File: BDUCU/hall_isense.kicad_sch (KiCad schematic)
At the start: 1 part, among them U6 LM358

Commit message: BDUCU did stuffs
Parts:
- added C15: 0.1uF, RMC_Capacitor:C_0805_2012Metric_Pad1.18x1.45mm_HandSolder_L, symbol Device:C
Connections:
- net HALL_HI_input: now reaches U6.5 (+)
- net HALL_HI: now reaches U6.6 (-)
- net HALL_HI: now also U6.7
- net GND: now reaches U6.4 (V-)
- net GND: now also C15.2
- net +5V: now reaches U6.8 (V+)
- net +5V: now also C15.1
- net HALL_LO: now reaches U6.1
- net HALL_LO: now also U6.2 (-)
- net HALL_LO_input: now reaches U6.3 (+)
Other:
- moved on the sheet: U6C
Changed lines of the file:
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@@
 (kicad_sch (version 20230121) (generator eeschema)
   (paper "A4")
-  (symbol (lib_id "Amplifier_Operational:LM358") (at 116.078 89.916 0) (unit 2)
-    (in_bom yes) (on_board yes) (dnp no) (fields_autoplaced)
-    (property "Reference" "U6" (at 116.078 80.01 0)
-      (effects (font (size 1.27 1.27)))
-    )
-    (property "Value" "LM358" (at 116.078 82.55 0)
-      (effects (font (size 1.27 1.27)))
-    )
-    (property "Footprint" "Package_SO:SOIC-8_3.9x4.9mm_P1.27mm" (at 116.078 89.916 0)
-      (effects (font (size 1.27 1.27)) hide)
-    )
-    (property "Datasheet" "http://www.ti.com/lit/ds/symlink/lm2904-n.pdf" (at 116.078 89.916 0)
+  (junction (at 149.86 38.1) (diameter 0) (color 0 0 0 0)
+  )
+  (junction (at 149.86 53.34) (diameter 0) (color 0 0 0 0)
+  )
+  (wire (pts (xy 144.145 53.34) (xy 149.86 53.34))
+    (stroke (width 0) (type default))
+  )
+  (wire (pts (xy 108.585 72.39) (xy 108.585 76.2))
+    (stroke (width 0) (type default))
+  )
+  (wire (pts (xy 144.145 42.545) (xy 144.145 38.1))
+    (stroke (width 0) (type default))
+  )
+  (wire (pts (xy 123.825 76.2) (xy 123.825 69.85))
+    (stroke (width 0) (type default))
+  )
+  (wire (pts (xy 108.585 76.2) (xy 123.825 76.2))
+    (stroke (width 0) (type default))
+  )
+  (wire (pts (xy 144.145 38.1) (xy 149.86 38.1))
+    (stroke (width 0) (type default))
+  )
+  (wire (pts (xy 108.585 97.79) (xy 123.825 97.79))
+    (stroke (width 0) (type default))
+  )
+  (wire (pts (xy 108.585 92.71) (xy 108.585 97.79))
+    (stroke (width 0) (type default))
+  )
+  (wire (pts (xy 123.825 97.79) (xy 123.825 90.17))
+    (stroke (width 0) (type default))
+  )
+  (wire (pts (xy 144.145 50.165) (xy 144.145 53.34))
+    (stroke (width 0) (type default))
+  )
+  (global_label "HALL_HI" (shape input) (at 123.825 90.17 0) (fields_autoplaced)
+    (effects (font (size 1.27 1.27)) (justify left))
+    (property "Intersheetrefs" "${INTERSHEET_REFS}" (at 134.1884 90.17 0)
+      (effects (font (size 1.27 1.27)) (justify left) hide)
+    )
+  )
+  (global_label "HALL_HI_input" (shape input) (at 108.585 87.63 180) (fields_autoplaced)
+    (effects (font (size 1.27 1.27)) (justify right))
+    (property "Intersheetrefs" "${INTERSHEET_REFS}" (at 92.4765 87.63 0)
+      (effects (font (size 1.27 1.27)) (justify right) hide)
+    )
+  )
+  (global_label "HALL_LO" (shape input) (at 123.825 69.85 0) (fields_autoplaced)
+    (effects (font (size 1.27 1.27)) (justify left))
+    (property "Intersheetrefs" "${INTERSHEET_REFS}" (at 134.6117 69.85 0)
+      (effects (font (size 1.27 1.27)) (justify left) hide)
+    )
+  )
+  (global_label "HALL_LO_input" (shape input) (at 108.585 67.31 180) (fields_autoplaced)
+    (effects (font (size 1.27 1.27)) (justify right))
+    (property "Intersheetrefs" "${INTERSHEET_REFS}" (at 92.0532 67.31 0)
+      (effects (font (size 1.27 1.27)) (justify right) hide)
+    )
+  )
+  (symbol (lib_id "power:GND") (at 149.86 53.34 0) (unit 1)
+    (in_bom yes) (on_board yes) (dnp no) (fields_autoplaced)
+    (property "Reference" "#PWR055" (at 149.86 59.69 0)
+      (effects (font (size 1.27 1.27)) hide)
+    )
+    (property "Value" "GND" (at 149.86 58.42 0)
+      (effects (font (size 1.27 1.27)))
+    )
+    (property "Footprint" "" (at 149.86 53.34 0)
+      (effects (font (size 1.27 1.27)) hide)
+    )
+    (property "Datasheet" "" (at 149.86 53.34 0)
+      (effects (font (size 1.27 1.27)) hide)
+    )
+    (pin "1")
+    (instances
+      (project "BDUCU"
+        (path "/9942a424-e19d-4ffb-8473-f960b5c811cf/8fc427df-2d97-44b9-b479-5014f2f05880/146987db-cc4e-40c2-bab5-0abba2715ce3"
+          (reference "#PWR055") (unit 1)
+        )
+        (path "/9942a424-e19d-4ffb-8473-f960b5c811cf/8fc427df-2d97-44b9-b479-5014f2f05880/e4047b2f-bef8-49d9-83e0-04d733111886"
+          (reference "#PWR058") (unit 1)
+        )
+        (path "/9942a424-e19d-4ffb-8473-f960b5c811cf/6945656a-1a27-4b96-8a88-6a11e7484dc7"
+          (reference "#PWR066") (unit 1)
+        )
+      )
+    )
+  )
+  (symbol (lib_id "Amplifier_Operational:LM358") (at 116.205 90.17 0) (unit 2)
+    (in_bom yes) (on_board yes) (dnp no) (fields_autoplaced)
+    (property "Reference" "U6" (at 116.205 80.264 0)
+      (effects (font (size 1.27 1.27)))
+    )
+    (property "Value" "LM358" (at 116.205 82.804 0)
+      (effects (font (size 1.27 1.27)))
+    )
+    (property "Footprint" "Package_SO:SOIC-8_3.9x4.9mm_P1.27mm" (at 116.205 90.17 0)
+      (effects (font (size 1.27 1.27)) hide)
+    )
+    (property "Datasheet" "http://www.ti.com/lit/ds/symlink/lm2904-n.pdf" (at 116.205 90.17 0)
       (effects (font (size 1.27 1.27)) hide)
     )
@@
     )
   )
-  (symbol (lib_id "Amplifier_Operational:LM358") (at 207.772 136.652 0) (unit 3)
-    (in_bom yes) (on_board yes) (dnp no) (fields_autoplaced)
-    (property "Reference" "U6" (at 207.01 135.382 0)
+  (symbol (lib_id "Device:C") (at 144.145 46.355 0) (unit 1)
+    (in_bom yes) (on_board yes) (dnp no)
+    (property "Reference" "C15" (at 140.081 45.085 0)
+      (effects (font (size 1.27 1.27)) (justify right))
+    )
+    (property "Value" "0.1uF" (at 140.081 47.625 0)
+      (effects (font (size 1.27 1.27)) (justify right))
+    )
+    (property "Footprint" "RMC_Capacitor:C_0805_2012Metric_Pad1.18x1.45mm_HandSolder_L" (at 145.1102 50.165 0)
+      (effects (font (size 1.27 1.27)) hide)
+    )
+    (property "Datasheet" "~" (at 144.145 46.355 0)
+      (effects (font (size 1.27 1.27)) hide)
+    )
+    (pin "1")
+    (pin "2")
+    (instances
+      (project "BDUCU"
+        (path "/9942a424-e19d-4ffb-8473-f960b5c811cf/d0210ccf-eb84-46ca-8cbf-aeaae330deeb"
+          (reference "C15") (unit 1)
+        )
+        (path "/9942a424-e19d-4ffb-8473-f960b5c811cf/6945656a-1a27-4b96-8a88-6a11e7484dc7"
+          (reference "C31") (unit 1)
+        )
+      )
+    )
+  )
+  (symbol (lib_id "power:+5V") (at 149.86 38.1 0) (unit 1)
+    (in_bom yes) (on_board yes) (dnp no) (fields_autoplaced)
+    (property "Reference" "#PWR014" (at 149.86 41.91 0)
+      (effects (font (size 1.27 1.27)) hide)
+    )
+    (property "Value" "+5V" (at 149.86 33.782 0)
+      (effects (font (size 1.27 1.27)))
+    )
+    (property "Footprint" "" (at 149.86 38.1 0)
+      (effects (font (size 1.27 1.27)) hide)
+    )
+    (property "Datasheet" "" (at 149.86 38.1 0)
+      (effects (font (size 1.27 1.27)) hide)
+    )
+    (pin "1")
+    (instances
+      (project "BDUCU"
+        (path "/9942a424-e19d-4ffb-8473-f960b5c811cf/d0210ccf-eb84-46ca-8cbf-aeaae330deeb"
+          (reference "#PWR014") (unit 1)
+        )
+        (path "/9942a424-e19d-4ffb-8473-f960b5c811cf/6945656a-1a27-4b96-8a88-6a11e7484dc7"
+          (reference "#PWR065") (unit 1)
+        )
+      )
+    )
+  )
+  (symbol (lib_id "Amplifier_Operational:LM358") (at 152.4 45.72 0) (unit 3)
+    (in_bom yes) (on_board yes) (dnp no) (fields_autoplaced)
+    (property "Reference" "U6" (at 151.638 44.45 0)
       (effects (font (size 1.27 1.27)) (justify left))
     )
-    (property "Value" "LM358" (at 207.01 137.922 0)
+    (property "Value" "LM358" (at 151.638 46.99 0)
       (effects (font (size 1.27 1.27)) (justify left))
     )
-    (property "Footprint" "Package_SO:SOIC-8_3.9x4.9mm_P1.27mm" (at 207.772 136.652 0)
-      (effects (font (size 1.27 1.27)) hide)
-    )
-    (property "Datasheet" "http://www.ti.com/lit/ds/symlink/lm2904-n.pdf" (at 207.772 136.652 0)
+    (property "Footprint" "Package_SO:SOIC-8_3.9x4.9mm_P1.27mm" (at 152.4 45.72 0)
+      (effects (font (size 1.27 1.27)) hide)
+    )
+    (property "Datasheet" "http://www.ti.com/lit/ds/symlink/lm2904-n.pdf" (at 152.4 45.72 0)
       (effects (font (size 1.27 1.27)) hide)
     )
@@
     )
   )
-  (symbol (lib_id "Amplifier_Operational:LM358") (at 116.332 69.85 0) (unit 1)
-    (in_bom yes) (on_board yes) (dnp no) (fields_autoplaced)
-    (property "Reference" "U6" (at 116.332 60.198 0)
-      (effects (font (size 1.27 1.27)))
-    )
-    (property "Value" "LM358" (at 116.332 62.738 0)
-      (effects (font (size 1.27 1.27)))
-    )
-    (property "Footprint" "Package_SO:SOIC-8_3.9x4.9mm_P1.27mm" (at 116.332 69.85 0)
-      (effects (font (size 1.27 1.27)) hide)
-    )
-    (property "Datasheet" "http://www.ti.com/lit/ds/symlink/lm2904-n.pdf" (at 116.332 69.85 0)
-      (effects (font (size 1.27 1.27)) hide)
-    )
+  (symbol (lib_id "Amplifier_Operational:LM358") (at 116.205 69.85 0) (unit 1)
+    (in_bom yes) (on_board yes) (dnp no) (fields_autoplaced)
+    (property "Reference" "U6" (at 116.205 60.198 0)
+      (effects (font (size 1.27 1.27)))
+    )
+    (property "Value" "LM358" (at 116.205 62.738 0)
+      (effects (font (size 1.27 1.27)))
+    )
+    (property "Footprint" "Package_SO:SOIC-8_3.9x4.9mm_P1.27mm" (at 116.205 69.85 0)
+      (effects (font (size 1.27 1.27)) hide)
+    )
+    (property "Datasheet" "http://www.ti.com/lit/ds/symlink/lm2904-n.pdf" (at 116.205 69.85 0)
+      (effects (font (size 1.27 1.27)) hide)
+    )

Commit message: weeeeeeee
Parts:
- renumbered C15 to C31

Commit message: bducu scheme done, waiting for check
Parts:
- C31: value 0.1uF -> 100nF
- U6: footprint Package_SO:SOIC-8_3.9x4.9mm_P1.27mm -> RMC_SO:SOIC-8_3.9x4.9mm_P1.27mm_RMC_Handsolder
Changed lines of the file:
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@@
 			)
 		)
-		(property "Footprint" "Package_SO:SOIC-8_3.9x4.9mm_P1.27mm"
+		(property "Footprint" "RMC_SO:SOIC-8_3.9x4.9mm_P1.27mm_RMC_Handsolder"
 			(at 116.205 90.17 0)
 			(effects
@@
 			)
 		)
-		(property "Value" "0.1uF"
+		(property "Value" "100nF"
 			(at 140.081 47.625 0)
 			(effects
@@
 			)
 		)
-		(property "Footprint" "Package_SO:SOIC-8_3.9x4.9mm_P1.27mm"
+		(property "Footprint" "RMC_SO:SOIC-8_3.9x4.9mm_P1.27mm_RMC_Handsolder"
 			(at 152.4 45.72 0)
 			(effects
@@
 			)
 		)
-		(property "Footprint" "Package_SO:SOIC-8_3.9x4.9mm_P1.27mm"
+		(property "Footprint" "RMC_SO:SOIC-8_3.9x4.9mm_P1.27mm_RMC_Handsolder"
 			(at 116.205 69.85 0)
 			(effects

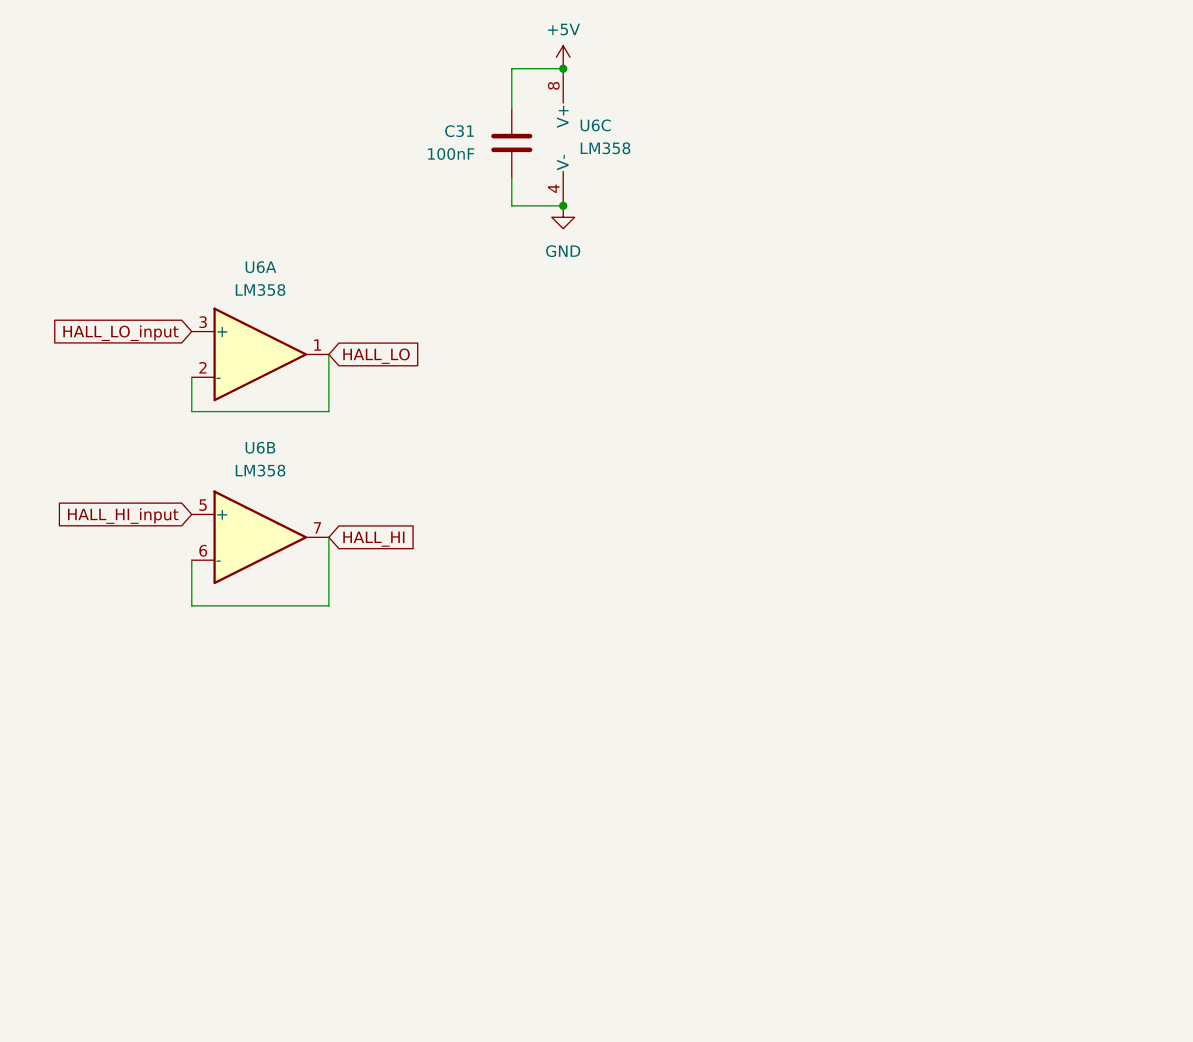
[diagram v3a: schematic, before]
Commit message: bducu done I think added ntc
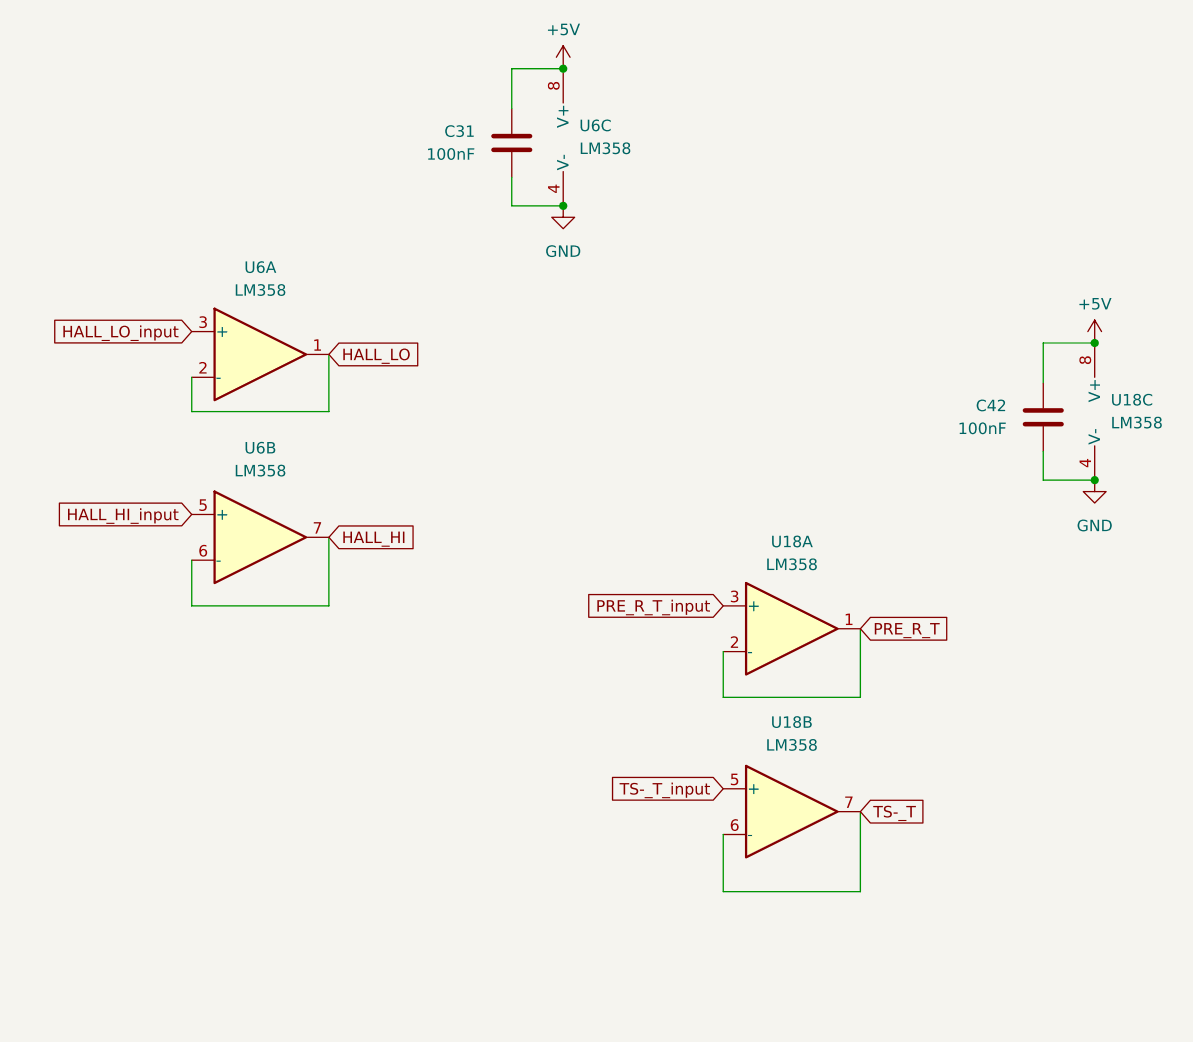
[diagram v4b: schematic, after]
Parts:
- added C42: 100nF, RMC_Capacitor:C_0805_2012Metric_Pad1.18x1.45mm_HandSolder_L, symbol Device:C
- added U18: LM358, RMC_SO:SOIC-8_3.9x4.9mm_P1.27mm_RMC_Handsolder, symbol Amplifier_Operational:LM358
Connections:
- net +5V: now also C42.1, U18.8 (V+)
- net GND: now also C42.2, U18.4 (V-)
- new net PRE_R_T: U18.1, U18.2 (-)
- new net PRE_R_T_input: U18.3 (+)
- new net TS-_T: U18.6 (-), U18.7
- new net TS-_T_input: U18.5 (+)

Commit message: bducu aiden please check
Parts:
- added R32, R37: 100k, RMC_Resistor:R_0805_2012Metric_Pad1.20x1.40mm_HandSolder_L, symbol Device:R
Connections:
- net GND: now also R32.1, R37.1
- net PRE_R_T_input: now also R32.2
- net TS-_T_input: now also R37.2

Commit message: I am Nicholas Chan (lesbian version)
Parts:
- renumbered C31 to C16, C42 to C17, R32 to R21, R37 to R22, U6 to U8, U18 to U9
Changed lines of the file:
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@@
 		(on_board yes)
 		(dnp no)
-		(property "Reference" "C42"
+		(property "Reference" "C17"
 			(at 199.136 75.565 0)
 			(effects
@@
 			(project "BDUCU"
 				(path "/9942a424-e19d-4ffb-8473-f960b5c811cf/6945656a-1a27-4b96-8a88-6a11e7484dc7"
-					(reference "C42")
+					(reference "C17")
 					(unit 1)
 				)
@@
 		(dnp no)
 		(fields_autoplaced yes)
-		(property "Reference" "#PWR066"
+		(property "Reference" "#PWR031"
 			(at 149.86 59.69 0)
 			(effects
@@
 			(project "BDUCU"
 				(path "/9942a424-e19d-4ffb-8473-f960b5c811cf/6945656a-1a27-4b96-8a88-6a11e7484dc7"
-					(reference "#PWR066")
+					(reference "#PWR031")
 					(unit 1)
 				)
@@
 		(dnp no)
 		(fields_autoplaced yes)
-		(property "Reference" "U18"
+		(property "Reference" "U9"
 			(at 175.26 90.678 0)
 			(effects
@@
 			(project "BDUCU"
 				(path "/9942a424-e19d-4ffb-8473-f960b5c811cf/6945656a-1a27-4b96-8a88-6a11e7484dc7"
-					(reference "U18")
+					(reference "U9")
 					(unit 1)
 				)
@@
 		(dnp no)
 		(fields_autoplaced yes)
-		(property "Reference" "U18"
+		(property "Reference" "U9"
 			(at 175.26 110.744 0)
 			(effects
@@
 			(project "BDUCU"
 				(path "/9942a424-e19d-4ffb-8473-f960b5c811cf/6945656a-1a27-4b96-8a88-6a11e7484dc7"
-					(reference "U18")
+					(reference "U9")
 					(unit 2)
 				)
@@
 		(dnp no)
 		(fields_autoplaced yes)
-		(property "Reference" "#PWR0301"
+		(property "Reference" "#PWR032"
 			(at 157.48 111.76 0)
 			(effects
@@
 			(project ""
 				(path "/9942a424-e19d-4ffb-8473-f960b5c811cf/6945656a-1a27-4b96-8a88-6a11e7484dc7"
-					(reference "#PWR0301")
+					(reference "#PWR032")
 					(unit 1)
 				)
@@
 		(dnp no)
 		(fields_autoplaced yes)
-		(property "Reference" "#PWR0302"
+		(property "Reference" "#PWR033"
 			(at 157.48 132.08 0)
 			(effects
@@
 			(project "BDUCU"
 				(path "/9942a424-e19d-4ffb-8473-f960b5c811cf/6945656a-1a27-4b96-8a88-6a11e7484dc7"
-					(reference "#PWR0302")
+					(reference "#PWR033")
 					(unit 1)
 				)
@@
 		(dnp no)
 		(fields_autoplaced yes)
-		(property "Reference" "U6"
+		(property "Reference" "U8"
 			(at 116.205 80.264 0)
 			(effects
@@
 			(project "BDUCU"
 				(path "/9942a424-e19d-4ffb-8473-f960b5c811cf/6945656a-1a27-4b96-8a88-6a11e7484dc7"
-					(reference "U6")
+					(reference "U8")
 					(unit 2)
 				)
@@
 		(on_board yes)
 		(dnp no)
-		(property "Reference" "R32"
+		(property "Reference" "R21"
 			(at 160.909 100.711 0)
 			(effects
@@
 			(project "BDUCU"
 				(path "/9942a424-e19d-4ffb-8473-f960b5c811cf/6945656a-1a27-4b96-8a88-6a11e7484dc7"
-					(reference "R32")
+					(reference "R21")
 					(unit 1)
 				)
@@
 		(on_board yes)
 		(dnp no)
-		(property "Reference" "C31"
+		(property "Reference" "C16"
 			(at 140.081 45.085 0)
 			(effects
@@
 			(project "BDUCU"
 				(path "/9942a424-e19d-4ffb-8473-f960b5c811cf/6945656a-1a27-4b96-8a88-6a11e7484dc7"
-					(reference "C31")
+					(reference "C16")
 					(unit 1)
 				)
@@
 		(on_board yes)
 		(dnp no)
-		(property "Reference" "R37"
+		(property "Reference" "R22"
 			(at 160.909 121.031 0)
 			(effects
@@
 			(project "BDUCU"
 				(path "/9942a424-e19d-4ffb-8473-f960b5c811cf/6945656a-1a27-4b96-8a88-6a11e7484dc7"
-					(reference "R37")
+					(reference "R22")
 					(unit 1)
 				)
@@
 		(dnp no)
 		(fields_autoplaced yes)
-		(property "Reference" "#PWR065"
+		(property "Reference" "#PWR030"
 			(at 149.86 41.91 0)
 			(effects
@@
 			(project "BDUCU"
 				(path "/9942a424-e19d-4ffb-8473-f960b5c811cf/6945656a-1a27-4b96-8a88-6a11e7484dc7"
-					(reference "#PWR065")
+					(reference "#PWR030")
 					(unit 1)
 				)
@@
 		(dnp no)
 		(fields_autoplaced yes)
-		(property "Reference" "U18"
+		(property "Reference" "U9"
 			(at 210.693 74.93 0)
 			(effects
@@
 			(project "BDUCU"
 				(path "/9942a424-e19d-4ffb-8473-f960b5c811cf/6945656a-1a27-4b96-8a88-6a11e7484dc7"
-					(reference "U18")
+					(reference "U9")
 					(unit 3)
 				)
@@
 		(dnp no)
 		(fields_autoplaced yes)
-		(property "Reference" "#PWR0122"
+		(property "Reference" "#PWR035"
 			(at 208.915 90.17 0)
 			(effects
@@
 			(project "BDUCU"
 				(path "/9942a424-e19d-4ffb-8473-f960b5c811cf/6945656a-1a27-4b96-8a88-6a11e7484dc7"
-					(reference "#PWR0122")
+					(reference "#PWR035")
 					(unit 1)
 				)
@@
 		(dnp no)
 		(fields_autoplaced yes)
-		(property "Reference" "#PWR0121"
+		(property "Reference" "#PWR034"
 			(at 208.915 72.39 0)
 			(effects
@@
 			(project "BDUCU"
 				(path "/9942a424-e19d-4ffb-8473-f960b5c811cf/6945656a-1a27-4b96-8a88-6a11e7484dc7"
-					(reference "#PWR0121")
+					(reference "#PWR034")
 					(unit 1)
 				)
@@
 		(dnp no)
 		(fields_autoplaced yes)
-		(property "Reference" "U6"
+		(property "Reference" "U8"
 			(at 151.638 44.45 0)
 			(effects
@@
 			(project "BDUCU"
 				(path "/9942a424-e19d-4ffb-8473-f960b5c811cf/6945656a-1a27-4b96-8a88-6a11e7484dc7"
-					(reference "U6")
+					(reference "U8")
 					(unit 3)
 				)
@@
 		(dnp no)
 		(fields_autoplaced yes)
-		(property "Reference" "U6"
+		(property "Reference" "U8"
 			(at 116.205 60.198 0)
 			(effects
@@
 			(project "BDUCU"
 				(path "/9942a424-e19d-4ffb-8473-f960b5c811cf/6945656a-1a27-4b96-8a88-6a11e7484dc7"
-					(reference "U6")
-					(unit 1)
-				)
+					(reference "U8")
+					(unit 1)
+				)
